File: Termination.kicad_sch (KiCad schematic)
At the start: 0 parts

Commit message: Update design
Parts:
- added C1, C3: 100uF, symbol Device:C_Small
- added C2, C4: 4.7uF, symbol Device:C_Polarized_Small
- added FL1, FL10, FL2, FL3, FL4, FL5, FL6, FL7, FL8, FL9: DA1206D600R-10, DA1206D600R-10:FB_DA1206D600R-10, symbol DA1206D600R-10:DA1206D600R-10
- added J1: Conn_02x25_Odd_Even, symbol Connector_Generic:Conn_02x25_Odd_Even
- added R4, R5: YC324-FK-071KL, YC324-FK-071KL:RESCAXS127P508X320X70-8N, symbol YC324-FK-071KL:YC324-FK-071KL
- added SW1: 219-8MST, SO16_219-8_CTS, symbol 219_8MST:219-8MST
- added U10: SN74F244DB, DB20, symbol SN74F244DB:SN74F244DB
- added U8, U9: ~, Package_SO:TSSOP-20_4.4x6.5mm_P0.65mm, symbol ds2107:DS21S07AE
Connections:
- new net: FL1.5, J1.44 (Pin_44)
- new net: FL1.6, J1.46 (Pin_46)
- new net: FL1.7, J1.48 (Pin_48)
- new net: FL1.8, J1.50 (Pin_50)
- new net: C3.1, C4.1, U9.19 (VREF2), U9.9 (VREF1)
- new net: C1.1, C2.1, U8.19 (VREF2), U8.9 (VREF1)
- new net: FL3.5, J1.14 (Pin_14)
- new net: FL3.6, J1.16 (Pin_16)
- new net: FL3.7, J1.18 (Pin_18)
- new net: FL3.8, J1.32 (Pin_32)
- new net: FL2.5, J1.36 (Pin_36)
- new net: FL2.6, J1.38 (Pin_38)
- new net: FL2.7, J1.40 (Pin_40)
- new net: FL2.8, J1.42 (Pin_42)
- new net: FL5.7, J1.2 (Pin_2)
- new net: FL5.8, J1.4 (Pin_4)
- new net: FL4.5, J1.6 (Pin_6)
- new net: FL4.6, J1.8 (Pin_8)
- new net: FL4.7, J1.10 (Pin_10)
- new net: FL4.8, J1.12 (Pin_12)
- new net D0: U10.3 (2Y4)
- new net D1: U10.5 (2Y3)
- new net D2: U10.7 (2Y2)
- new net D3: U10.9 (2Y1)
- new net D4: U10.12 (1Y4)
- new net D5: U10.14 (1Y3)
- new net D6: U10.16 (1Y2)
- new net D7: U10.18 (1Y1)
- new net DIP_EXT_TERM: R5.3, SW1.7, U10.4 (1A2), U8.20 (~{PD}), U9.20 (~{PD})
- new net DIP_LONG_SPINUP: R5.1, SW1.5, U10.8 (1A4)
- new net DIP_SCSI_ADDR0: R4.1, SW1.1, U10.17 (2A4)
- new net DIP_SCSI_ADDR1: R4.2, SW1.2, U10.15 (2A3)
- new net DIP_SCSI_ADDR2: R4.3, SW1.3, U10.13 (2A2)
- new net DIP_SCSI_FAST: R4.4, SW1.4, U10.11 (2A1)
- new net DIP_SCSI_LUNS: R5.4, SW1.8, U10.2 (1A1)
- new net DIP_SYNCH_MODE: R5.2, SW1.6, U10.6 (1A3)
- new net GND: C1.2, C2.2, C3.2, C4.2, J1.1 (Pin_1), J1.11 (Pin_11), J1.13 (Pin_13), J1.15 (Pin_15), J1.17 (Pin_17), J1.19 (Pin_19), J1.20 (Pin_20), J1.21 (Pin_21), J1.22 (Pin_22), J1.23 (Pin_23), J1.24 (Pin_24), J1.27 (Pin_27), J1.28 (Pin_28), J1.29 (Pin_29), J1.3 (Pin_3), J1.30 (Pin_30), J1.31 (Pin_31), J1.33 (Pin_33), J1.35 (Pin_35), J1.37 (Pin_37), J1.39 (Pin_39), J1.41 (Pin_41), J1.43 (Pin_43), J1.45 (Pin_45), J1.47 (Pin_47), J1.49 (Pin_49), J1.5 (Pin_5), J1.7 (Pin_7), J1.9 (Pin_9), SW1.10, SW1.11, SW1.12, SW1.13, SW1.14, SW1.15, SW1.16, SW1.9, U10.10 (GND), U8.10 (GND), U9.10 (GND)
- new net PLD_SID: U10.1 (*1OE), U10.19 (*2OE)
- new net SCDAT0: FL10.1, FL5.2, U8.4 (R2)
- new net SCDAT1: FL10.2, FL5.1, U8.5 (R3)
- new net SCDAT2: FL10.3, FL4.4, U8.6 (R4)
- new net SCDAT3: FL10.4, FL4.3, U8.7 (R5)
- new net SCDAT4: FL4.2, FL9.1, U9.6 (R4)
- new net SCDAT5: FL4.1, FL9.2, U8.13 (R6)
- new net SCDAT6: FL3.4, FL9.3, U8.14 (R7)
- new net SCDAT7: FL3.3, FL9.4, U8.15 (R8)
- new net SCDATP: FL3.2, FL8.1, U8.16 (R9)
- new net SCSI_TERMPWR: J1.26 (Pin_26), U8.1 (TPWR1), U8.11 (TPWR2), U9.1 (TPWR1), U9.11 (TPWR2)
- new net SCTRL_ACK: FL2.3, FL8.4, U9.13 (R6)
- new net SCTRL_ATN: FL3.1, FL8.2, U9.7 (R5)
- new net SCTRL_BSY: FL2.4, FL8.3, U9.3 (R1)
- new net SCTRL_CD: FL1.3, FL6.4, U8.3 (R1)
- new net SCTRL_IO: FL1.1, FL7.2, U9.16 (R9)
- new net SCTRL_MSG: FL2.1, FL6.2, U9.15 (R8)
- new net SCTRL_REQ: FL1.2, FL7.1, U9.14 (R7)
- new net SCTRL_RST: FL2.2, FL6.1, U9.5 (R3)
- new net SCTRL_SEL: FL1.4, FL6.3, U9.4 (R2)
- new net V5: R4.5, R4.6, R4.7, R4.8, R5.5, R5.6, R5.7, R5.8, U10.20 (VCC)
- no-connect marks 0 -> 2
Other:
- note added: "Active Termination"
- note added: "External Dip Switch"
- note added: "Internal 2x25 Connector"

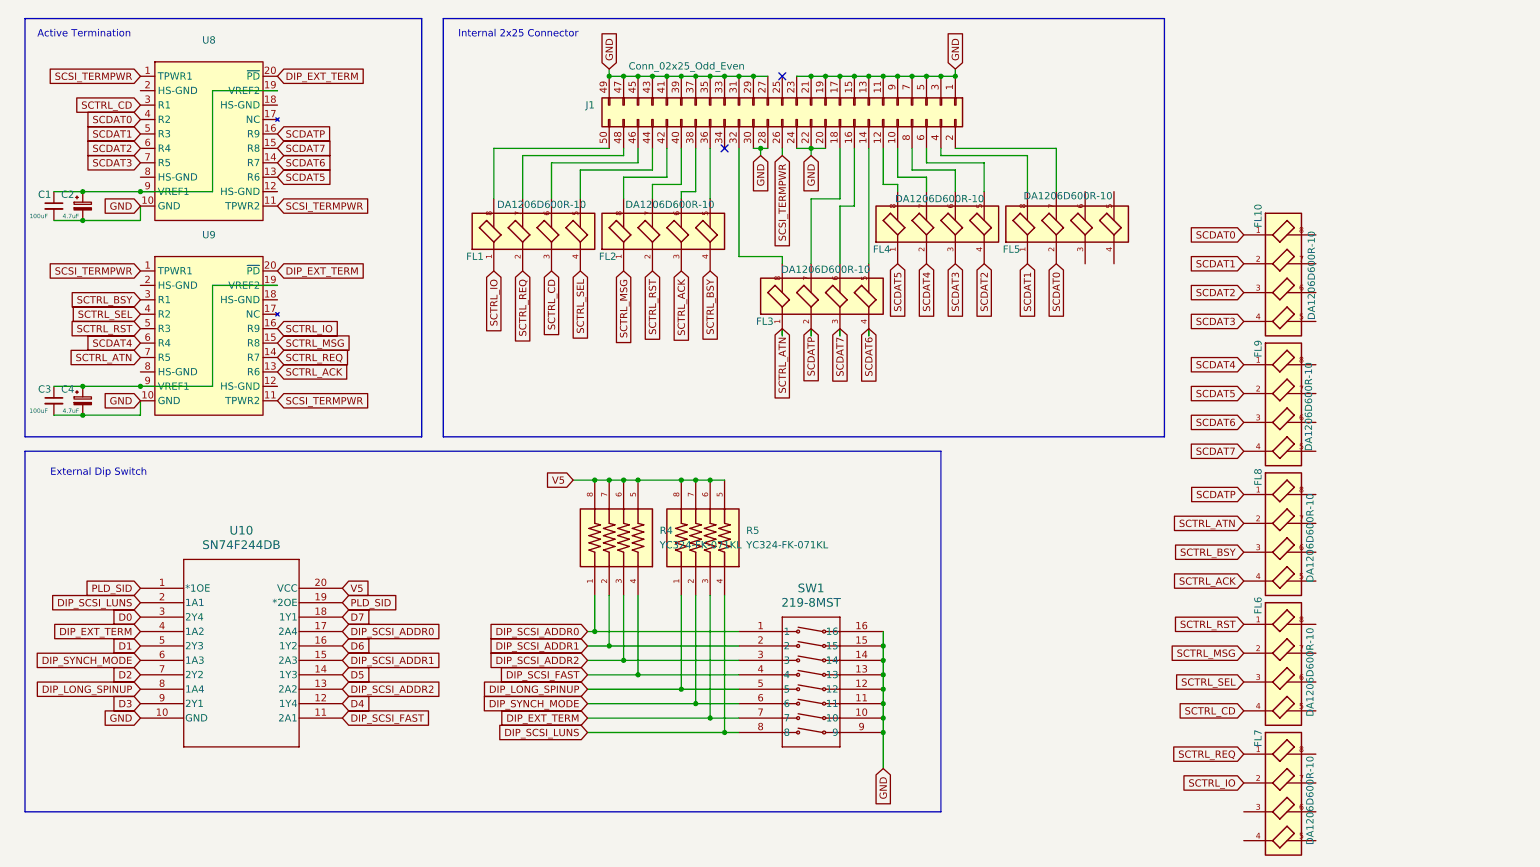
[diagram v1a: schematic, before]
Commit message: Redraw footprints, finish Termination/Connectors
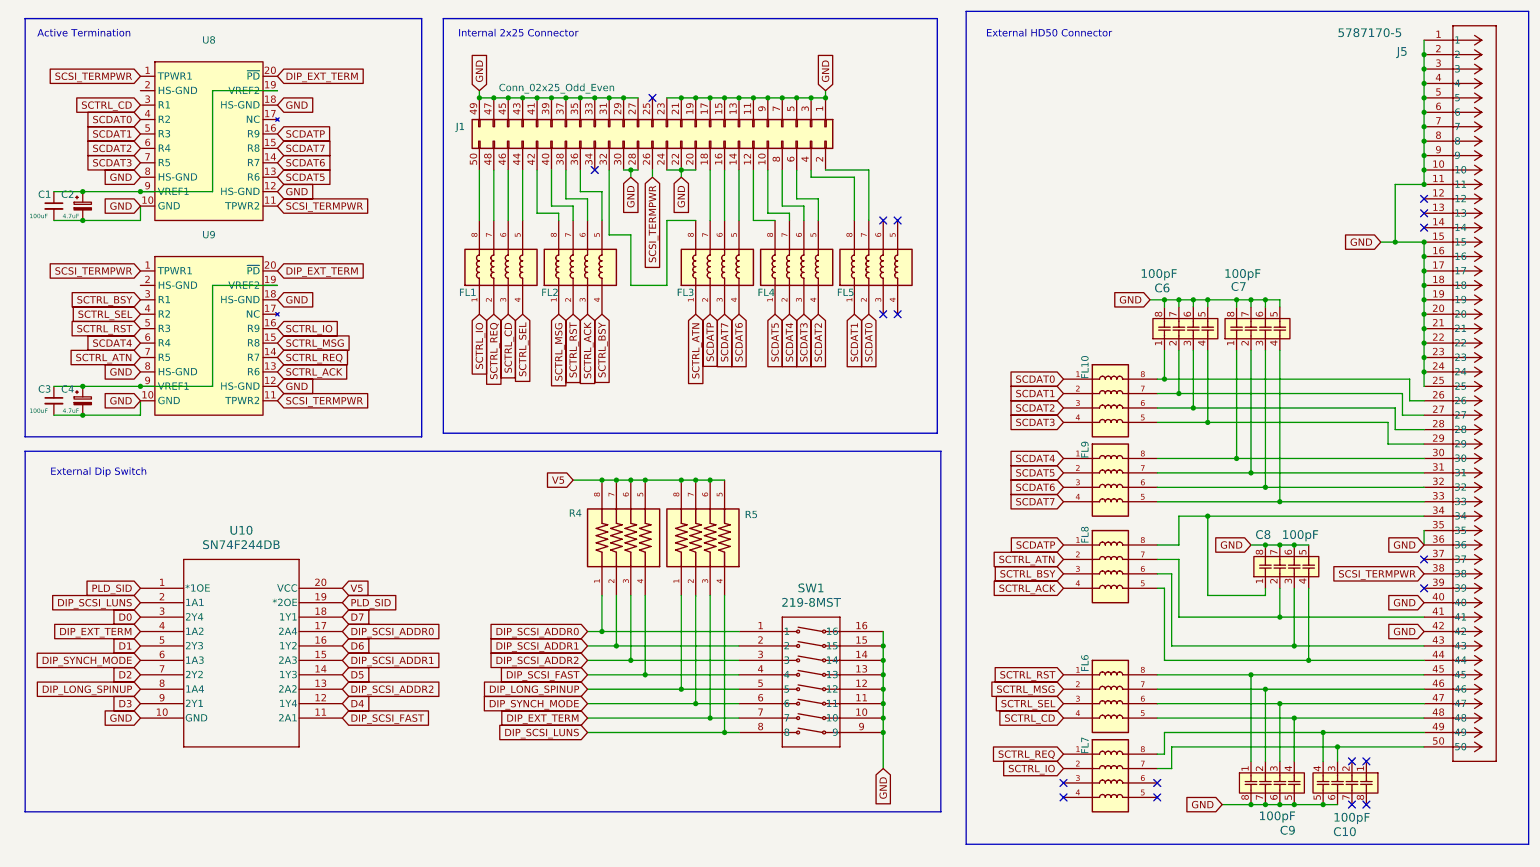
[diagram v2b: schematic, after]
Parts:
- added C10, C6, C7, C8, C9: 100pF, CAP_CA0612_3P2X1P6_YAG, symbol CA0612KRNPO9BN101:CA0612KRNPO9BN101
- added J5: 5787170-5, CONN_5787170-5_TYC, symbol 5787170_5:5787170-5
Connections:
- net GND: now also U8.12 (HS-GND), U8.18 (HS-GND), U8.8 (HS-GND), U9.12 (HS-GND), U9.18 (HS-GND), U9.8 (HS-GND), C10.5, C10.6, C6.5, C6.6, C6.7, C6.8, C7.5, C7.6, C7.7, C7.8, C8.5, C8.6, C8.7, C8.8, C9.5, C9.6, C9.7, C9.8, J5.1, J5.10, J5.11, J5.15, J5.16, J5.17, J5.18, J5.19, J5.2, J5.20, J5.21, J5.22, J5.23, J5.24, J5.25, J5.3, J5.35, J5.36, J5.4, J5.40, J5.42, J5.5, J5.6, J5.7, J5.8, J5.9
- net SCSI_TERMPWR: now also J5.38
- net at FL8.5: now also C8.4, J5.44
- net at FL8.6: now also C8.3, J5.43
- net at FL8.7: now also C8.2, J5.41
- net at FL8.8: now also C8.1, J5.34
- net at FL6.5: now also C9.4, J5.48
- net at FL6.6: now also C9.3, J5.47
- net at FL6.7: now also C9.2, J5.46
- net at FL6.8: now also C9.1, J5.45
- net at FL7.7: now also C10.3, J5.50
- net at FL7.8: now also C10.4, J5.49
- net at FL10.5: now also C6.4, J5.29
- net at FL10.6: now also C6.3, J5.28
- net at FL10.7: now also C6.2, J5.27
- net at FL10.8: now also C6.1, J5.26
- net at FL9.5: now also C7.4, J5.33
- net at FL9.6: now also C7.3, J5.32
- net at FL9.7: now also C7.2, J5.31
- net at FL9.8: now also C7.1, J5.30
- no-connect marks 2 -> 19
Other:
- note added: "External HD50 Connector"
- moved on the sheet: J1, R4

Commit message: More work. Getting there.
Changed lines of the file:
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@@
 	(rectangle
 		(start 16.51 91.44)
-		(end 177.8 154.94)
+		(end 177.165 160.655)
 		(stroke
 			(width 0)

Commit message: Latest updates
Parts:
- C1, C3: value 100uF -> 100nF; footprint (none) -> Capacitor_SMD:C_0603_1608Metric_Pad1.08x0.95mm_HandSolder
- C10, C6, C7, C8, C9: footprint CAP_CA0612_3P2X1P6_YAG -> CA0612KRNPO9BN101:CAP_CA0612_3P2X1P6_YAG
- C2, C4: footprint (none) -> Capacitor_SMD:CP_Elec_4x5.7
- J1: footprint (none) -> Connector_IDC:IDC-Header_2x25_P2.54mm_Vertical
- J5: footprint CONN_5787170-5_TYC -> 5787170_5:CONN_5787170-5_TYC
- SW1: footprint SO16_219-8_CTS -> 219_8MST:SO16_219-8_CTS
- U10: footprint DB20 -> SN74F244DB:DB20
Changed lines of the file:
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@@
 			)
 		)
-		(property "Footprint" "CONN_5787170-5_TYC"
+		(property "Footprint" "5787170_5:CONN_5787170-5_TYC"
 			(at 262.89 19.05 0)
 			(effects
@@
 			)
 		)
-		(property "Datasheet" "5787170-5"
+		(property "Datasheet" "https://www.te.com/commerce/DocumentDelivery/DDEController?Action=srchrtrv&DocNm=1-1773938-5_AMPLIMITE_.050_Series_QRG&DocType=Data+Sheet&DocLang=English&DocFormat=pdf&PartCntxt=5787170-5"
 			(at 262.89 19.05 0)
 			(effects
@@
 			)
 		)
-		(property "Footprint" "CAP_CA0612_3P2X1P6_YAG"
+		(property "Footprint" "CA0612KRNPO9BN101:CAP_CA0612_3P2X1P6_YAG"
 			(at 249.936 110.744 0)
 			(effects
@@
 			)
 		)
-		(property "Footprint" "CAP_CA0612_3P2X1P6_YAG"
+		(property "Footprint" "CA0612KRNPO9BN101:CAP_CA0612_3P2X1P6_YAG"
 			(at 247.396 150.876 0)
 			(effects
@@
 			)
 		)
-		(property "Value" "100uF"
+		(property "Value" "100nF"
 			(at 17.272 84.328 0)
 			(effects
@@
 			)
 		)
-		(property "Footprint" ""
+		(property "Footprint" "Capacitor_SMD:C_0603_1608Metric_Pad1.08x0.95mm_HandSolder"
 			(at 21.59 82.55 0)
 			(effects
@@
 			)
 		)
-		(property "Footprint" "SO16_219-8_CTS"
+		(property "Footprint" "219_8MST:SO16_219-8_CTS"
 			(at 142.24 123.19 0)
 			(effects
@@
 			)
 		)
-		(property "Footprint" ""
+		(property "Footprint" "Capacitor_SMD:CP_Elec_4x5.7"
 			(at 26.67 48.26 0)
 			(effects
@@
 			)
 		)
-		(property "Footprint" ""
+		(property "Footprint" "Capacitor_SMD:CP_Elec_4x5.7"
 			(at 26.67 82.55 0)
 			(effects
@@
 			)
 		)
-		(property "Footprint" "CAP_CA0612_3P2X1P6_YAG"
+		(property "Footprint" "CA0612KRNPO9BN101:CAP_CA0612_3P2X1P6_YAG"
 			(at 232.156 68.834 0)
 			(effects
@@
 			)
 		)
-		(property "Footprint" "CAP_CA0612_3P2X1P6_YAG"
+		(property "Footprint" "CA0612KRNPO9BN101:CAP_CA0612_3P2X1P6_YAG"
 			(at 244.856 68.834 0)
 			(effects
@@
 			)
 		)
-		(property "Footprint" "DB20"
+		(property "Footprint" "SN74F244DB:DB20"
 			(at 24.13 115.57 0)
 			(effects
@@
 			)
 		)
-		(property "Value" "100uF"
+		(property "Value" "100nF"
 			(at 17.272 50.038 0)
 			(effects
@@
 			)
 		)
-		(property "Footprint" ""
+		(property "Footprint" "Capacitor_SMD:C_0603_1608Metric_Pad1.08x0.95mm_HandSolder"
 			(at 21.59 48.26 0)
 			(effects
@@
 			)
 		)
-		(property "Footprint" "CAP_CA0612_3P2X1P6_YAG"
+		(property "Footprint" "CA0612KRNPO9BN101:CAP_CA0612_3P2X1P6_YAG"
 			(at 237.744 150.876 0)
 			(effects
@@
 			)
 		)
-		(property "Footprint" ""
+		(property "Footprint" "Connector_IDC:IDC-Header_2x25_P2.54mm_Vertical"
 			(at 127 34.29 0)
 			(effects

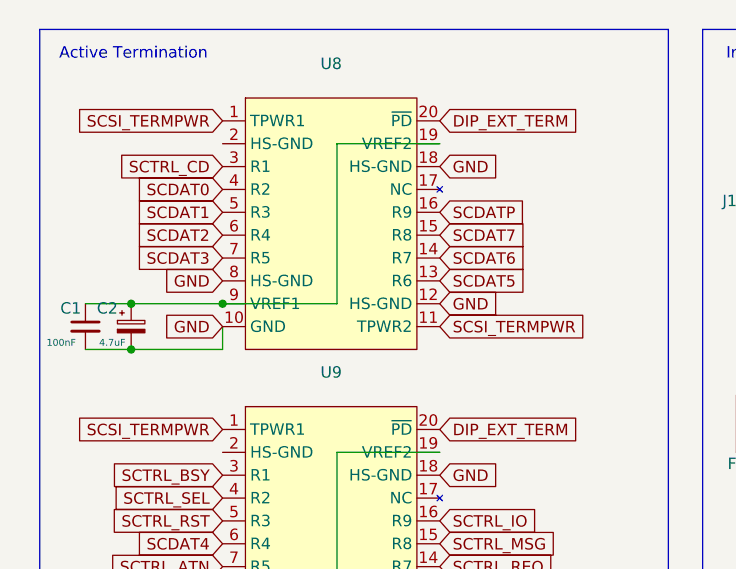
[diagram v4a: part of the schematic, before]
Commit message: Finished first pass at new schematics
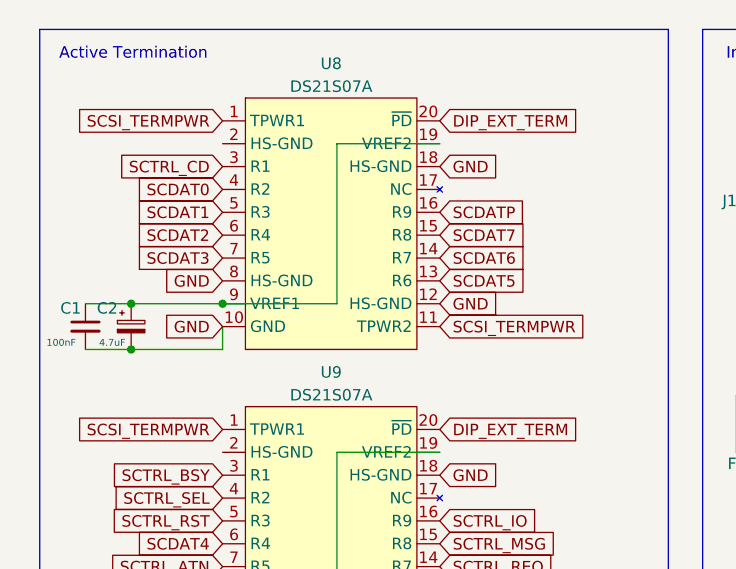
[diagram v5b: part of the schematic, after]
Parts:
- U8, U9: value ~ -> DS21S07A
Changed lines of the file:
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@@
 			)
 		)
-		(property "Value" "~"
+		(property "Value" "DS21S07A"
 			(at 48.895 55.88 0)
 			(effects
@@
 			)
 		)
-		(property "Value" "~"
+		(property "Value" "DS21S07A"
 			(at 48.895 21.59 0)
 			(effects

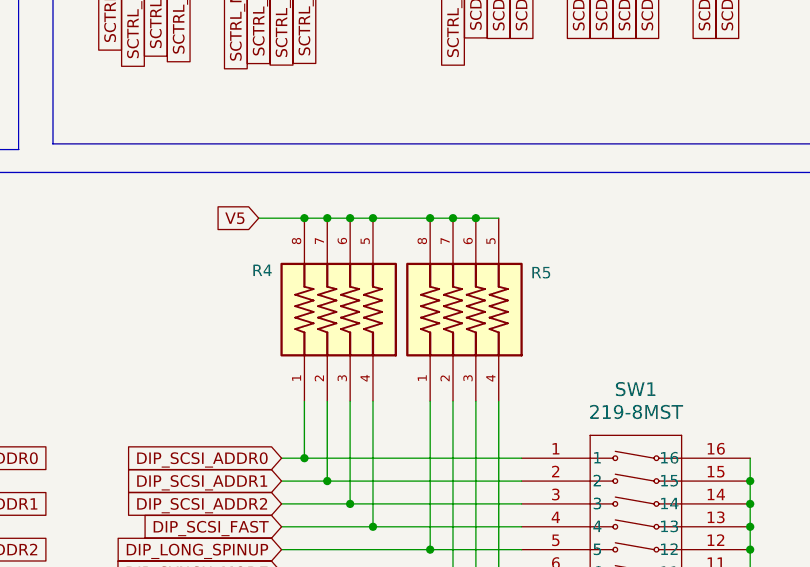
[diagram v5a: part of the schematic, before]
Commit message: Update RN footprint to CAY16_102J4LF
- Rename RNs from R to RN.
- Fix U5 footprint
- Rename pages to be consecutive numbers
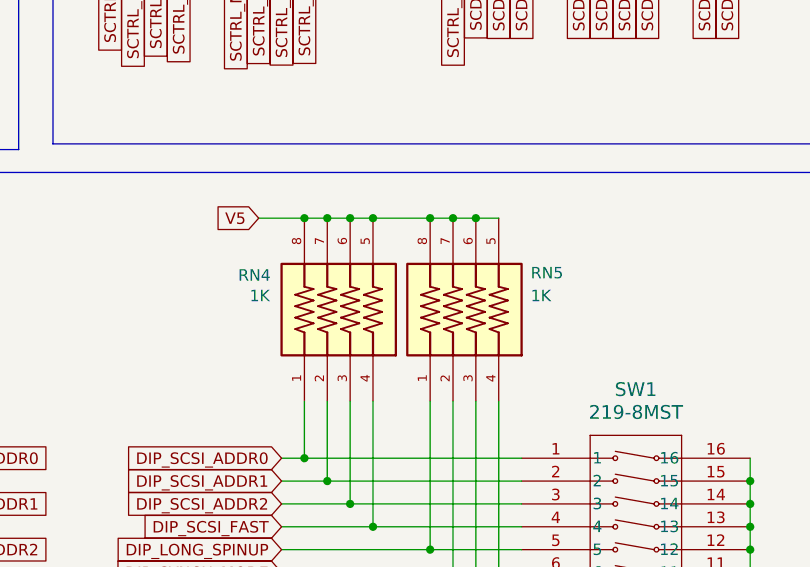
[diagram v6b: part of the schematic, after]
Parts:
- RN4: renamed from R4; value YC324-FK-071KL -> 1K; footprint YC324-FK-071KL:RESCAXS127P508X320X70-8N -> CAY16_102J4LF:BO_CAY16
- RN5: renamed from R5; value YC324-FK-071KL -> 1K; footprint YC324-FK-071KL:RESCAXS127P508X320X70-8N -> CAY16_102J4LF:BO_CAY16
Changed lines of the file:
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@@
 		(on_board yes)
 		(dnp no)
-		(property "Reference" "R4"
-			(at 112.268 102.362 90)
+		(property "Reference" "RN4"
+			(at 110.744 102.87 90)
 			(effects
 				(font
@@
 			)
 		)
-		(property "Value" "YC324-FK-071KL"
-			(at 129.54 107.9499 90)
+		(property "Value" "1K"
+			(at 112.014 105.156 90)
 			(effects
 				(font
@@
 				)
 				(justify right)
-				(hide yes)
-			)
-		)
-		(property "Footprint" "YC324-FK-071KL:RESCAXS127P508X320X70-8N"
+			)
+		)
+		(property "Footprint" "CAY16_102J4LF:BO_CAY16"
 			(at 123.19 106.68 0)
 			(effects
@@
 			(project ""
 				(path "/8f9f4021-47aa-41d9-bea7-f6ccf72098bb/53e9e23b-3b92-4a87-a15c-9c224d6145c5"
-					(reference "R4")
+					(reference "RN4")
 					(unit 1)
 				)
@@
 		(on_board yes)
 		(dnp no)
-		(property "Reference" "R5"
+		(property "Reference" "RN5"
 			(at 143.256 102.616 90)
 			(effects
@@
 			)
 		)
-		(property "Value" "YC324-FK-071KL"
-			(at 143.51 107.9499 90)
+		(property "Value" "1K"
+			(at 143.256 105.156 90)
 			(effects
 				(font
@@
 				)
 				(justify right)
-				(hide yes)
-			)
-		)
-		(property "Footprint" "YC324-FK-071KL:RESCAXS127P508X320X70-8N"
+			)
+		)
+		(property "Footprint" "CAY16_102J4LF:BO_CAY16"
 			(at 137.16 106.68 0)
 			(effects
@@
 			(project ""
 				(path "/8f9f4021-47aa-41d9-bea7-f6ccf72098bb/53e9e23b-3b92-4a87-a15c-9c224d6145c5"
-					(reference "R5")
+					(reference "RN5")
 					(unit 1)
 				)
